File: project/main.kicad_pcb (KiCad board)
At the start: 6 copper layers, 160 x 257 mm, 207 parts

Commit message: extra comms and power towards hallway
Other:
- board text added: "201"
- board text added: "202"
- board text added: "203"
- board text added: "204"
- board text added: "215"
- board text added: "216"
- board text added: "3x2.5 C16 8m 3x"
- board text added: "D313"
- board text added: "PDU-A1 and PDU-A2 - 2x23m"
- board text added: "PDU-B1 and PDU-B2 - 2x16m"
- board text added: "cam-el2 27m"
- board text added: "print-dfm1 21m"
- board text added: "print-dfm2 21m"
- board text added: "print-sla1 17m"
- board text removed: "???"
- board text removed: "PDU-A-1 and PDU-A-2 - 2x22m"
- board text removed: "PDU-B-1 and PDU-B-2 - 2x15m"
- board text removed: "cam-el2 11m"
- board text removed: "print-dfm1 19m"
- board text removed: "print-dfm2 19m"

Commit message: updating ventilation map
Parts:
- added R105: machine intake fan, -local:_q_laser_fan__, F.Cu at (78.3, 43.8)
- added R106: heat exchanger, -local:_q_printers_fan__, F.Cu at (83.8, 165.3)
- added R107: dirty big fan, -local:_q_paint_fan__, F.Cu at (78.3, 97.3)
- R101: value Laser fan -> laser fan
- R102: value Paint fan -> dirty fan
- R103: value Printers fan -> air con
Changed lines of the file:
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@@
   (net 110 "unconnected-(R99-Pad1)")
   (net 111 "unconnected-(R52-Pad1)")
+  (net 112 "unconnected-(R105-Pad1)")
+  (net 113 "unconnected-(R106-Pad1)")
+  (net 114 "unconnected-(R107-Pad1)")
   (footprint "-local:_o_lathe__" (layer "F.Cu")
     (at 112.28 26)
@@
     )
   )
+  (footprint "-local:_q_paint_fan__" (layer "F.Cu")
+    (at 78.28 97.32 90)
+    (property "Sheetfile" "main.kicad_sch")
+    (property "Sheetname" "")
+    (attr smd)
+    (fp_text reference "R107" (at -0.5 -1.5 90 unlocked) (layer "F.Fab")
+      (effects (font (size 0.8 0.8) (thickness 0.08)) (justify left))
+    )
+    (fp_text value "dirty big fan" (at 0.5 3 90 unlocked) (layer "F.SilkS")
+      (effects (font (size 0.8 0.8) (thickness 0.08)) (justify left))
+    )
+    (fp_text user "${REFERENCE}" (at 1.5 -3 90 unlocked) (layer "F.Fab")
+      (effects (font (size 1 1) (thickness 0.15)))
+    )
+    (fp_rect (start 0 0) (end 3 2) (layer "F.SilkS") (width 0.12) (fill none))
+    (fp_rect (start -0.5 -0.5) (end 3.5 2.5) (layer "F.CrtYd") (width 0.05) (fill none))
+    (pad "1" smd roundrect (at 1.5 1 90) (size 3 2) (layers "F.Cu" "F.Paste" "F.Mask") (roundrect_rratio 0.1)
+      (net 114 "unconnected-(R107-Pad1)") (pintype "passive"))
+    (model "${KIPRJMOD}/lib/model/cube_1x1x1_mm.step"
+      (offset (xyz 1.5 -1 15))
+      (scale (xyz 3 2 3))
+      (rotate (xyz 0 0 0))
+    )
+  )
   (footprint "-local:chair_small" (layer "F.Cu")
     (at 148.5 194.25 -90)
@@
       (effects (font (size 0.8 0.8) (thickness 0.08)) (justify left))
     )
-    (fp_text value "Laser fan" (at 0.5 3 90 unlocked) (layer "F.SilkS")
+    (fp_text value "laser fan" (at 0.5 3 90 unlocked) (layer "F.SilkS")
       (effects (font (size 0.8 0.8) (thickness 0.08)) (justify left))
     )
@@
       (effects (font (size 0.8 0.8) (thickness 0.08)) (justify left))
     )
-    (fp_text value "Paint fan" (at 0.5 3 90 unlocked) (layer "F.SilkS")
+    (fp_text value "dirty fan" (at 0.5 3 90 unlocked) (layer "F.SilkS")
       (effects (font (size 0.8 0.8) (thickness 0.08)) (justify left))
     )
@@
     )
   )
+  (footprint "-local:_q_laser_fan__" (layer "F.Cu")
+    (at 78.28 43.82 90)
+    (property "Sheetfile" "main.kicad_sch")
+    (property "Sheetname" "")
+    (attr smd)
+    (fp_text reference "R105" (at -0.5 -1.5 90 unlocked) (layer "F.Fab")
+      (effects (font (size 0.8 0.8) (thickness 0.08)) (justify left))
+    )
+    (fp_text value "machine intake fan" (at 0.5 3 90 unlocked) (layer "F.SilkS")
+      (effects (font (size 0.8 0.8) (thickness 0.08)) (justify left))
+    )
+    (fp_text user "${REFERENCE}" (at 1.5 -3 90 unlocked) (layer "F.Fab")
+      (effects (font (size 1 1) (thickness 0.15)))
+    )
+    (fp_rect (start 0 0) (end 3 2) (layer "F.SilkS") (width 0.12) (fill none))
+    (fp_rect (start -0.5 -0.5) (end 3.5 2.5) (layer "F.CrtYd") (width 0.05) (fill none))
+    (pad "1" smd roundrect (at 1.5 1 90) (size 3 2) (layers "F.Cu" "F.Paste" "F.Mask") (roundrect_rratio 0.1)
+      (net 112 "unconnected-(R105-Pad1)") (pintype "passive"))
+    (model "${KIPRJMOD}/lib/model/cube_1x1x1_mm.step"
+      (offset (xyz 1.5 -1 15))
+      (scale (xyz 3 2 3))
+      (rotate (xyz 0 0 0))
+    )
+  )
   (footprint "-local:chair_small" (layer "F.Cu")
     (at 148.5 199.25 -90)
@@
     )
   )
+  (footprint "-local:_q_printers_fan__" (layer "F.Cu")
+    (at 83.78 165.32)
+    (property "Sheetfile" "main.kicad_sch")
+    (property "Sheetname" "")
+    (attr smd)
+    (fp_text reference "R106" (at -0.5 -1.5 unlocked) (layer "F.Fab")
+      (effects (font (size 0.8 0.8) (thickness 0.08)) (justify left))
+    )
+    (fp_text value "heat exchanger" (at 0.5 3 unlocked) (layer "F.SilkS")
+      (effects (font (size 0.8 0.8) (thickness 0.08)) (justify left))
+    )
+    (fp_text user "${REFERENCE}" (at 1.5 -3 unlocked) (layer "F.Fab")
+      (effects (font (size 1 1) (thickness 0.15)))
+    )
+    (fp_rect (start 0 0) (end 3 2) (layer "F.SilkS") (width 0.12) (fill none))
+    (fp_rect (start -0.5 -0.5) (end 3.5 2.5) (layer "F.CrtYd") (width 0.05) (fill none))
+    (pad "1" smd roundrect (at 1.5 1) (size 3 2) (layers "F.Cu" "F.Paste" "F.Mask") (roundrect_rratio 0.1)
+      (net 113 "unconnected-(R106-Pad1)") (pintype "passive"))
+    (model "${KIPRJMOD}/lib/model/cube_1x1x1_mm.step"
+      (offset (xyz 1.5 -1 15))
+      (scale (xyz 3 2 3))
+      (rotate (xyz 0 0 0))
+    )
+  )
   (footprint "-local:_o_thick_shelf__" (layer "F.Cu")
     (at 196.78 117.87 180)
@@
       (effects (font (size 0.8 0.8) (thickness 0.08)) (justify left))
     )
-    (fp_text value "Printers fan" (at 0.5 3 90 unlocked) (layer "F.SilkS")
+    (fp_text value "air con" (at 0.5 3 90 unlocked) (layer "F.SilkS")
       (effects (font (size 0.8 0.8) (thickness 0.08)) (justify left))
     )
@@
   )
   (gr_line (start 194.28 54.32) (end 194.28 62.32) (layer "In2.Cu") (width 5))
-  (gr_line (start 173.28 176.32) (end 194.28 176.32) (layer "In2.Cu") (width 3))
-  (gr_line (start 173.28 176.32) (end 173.28 172.32) (layer "In2.Cu") (width 3))
-  (gr_line (start 199.28 121.32) (end 194.28 121.32) (layer "In2.Cu") (width 3))
+  (gr_line (start 191.28 179.32) (end 194.28 179.32) (layer "In2.Cu") (width 3))
+  (gr_line (start 191.28 182.32) (end 191.28 179.32) (layer "In2.Cu") (width 3))
+  (gr_line (start 199.28 133.32) (end 194.28 133.32) (layer "In2.Cu") (width 3))
   (gr_line (start 90.28 31.32) (end 90.28 26.32) (layer "In2.Cu") (width 2))
   (gr_line (start 181.28 54.32) (end 194.28 54.32) (layer "In2.Cu") (width 5))
-  (gr_line (start 173.28 180.32) (end 173.28 176.32) (layer "In2.Cu") (width 1))
-  (gr_line (start 173.28 180.32) (end 152.28 180.32) (layer "In2.Cu") (width 1))
+  (gr_line (start 188.28 179.32) (end 191.28 179.32) (layer "In2.Cu") (width 1))
+  (gr_line (start 199.28 71.32) (end 194.28 71.32) (layer "In2.Cu") (width 3))
   (gr_line (start 194.28 62.32) (end 199.28 62.32) (layer "In2.Cu") (width 5))
   (gr_line (start 164.28 31.32) (end 164.28 26.32) (layer "In2.Cu") (width 2))
   (gr_line (start 90.28 31.32) (end 171.28 31.32) (layer "In2.Cu") (width 2))
-  (gr_line (start 171.28 31.32) (end 171.28 53.32) (layer "In2.Cu") (width 2))
-  (gr_line (start 194.28 176.32) (end 194.28 62.32) (layer "In2.Cu") (width 3))
+  (gr_line (start 194.28 179.32) (end 194.28 62.32) (layer "In2.Cu") (width 3))
   (gr_line (start 169.28 26.32) (end 169.28 57.32) (layer "In3.Cu") (width 1))
   (gr_arc (start 119.28 119.32) (mid 116.351068 126.391068) (end 109.28 129.32) (layer "In3.Cu") (width 0.2))
@@
   (gr_line (start 109.28 129.32) (end 109.28 119.32) (layer "In3.Cu") (width 0.2))
   (gr_line (start 201.28 179.82) (end 126.28 179.82) (layer "In3.Cu") (width 0.5))
+  (gr_line (start 196.28 30.32) (end 196.28 60.32) (layer "In4.Cu") (width 1.6))
+  (gr_line (start 196.28 30.32) (end 155.28 30.32) (layer "In4.Cu") (width 1.6))
+  (gr_line (start 156.28 92.32) (end 156.28 63.32) (layer "In4.Cu") (width 2))
+  (gr_line (start 79.28 42.32) (end 84.28 42.32) (layer "In4.Cu") (width 2))
+  (gr_line (start 83.28 155.32) (end 79.28 155.32) (layer "In4.Cu") (width 2.5))
+  (gr_line (start 105.28 173.32) (end 105.28 181.32) (layer "In4.Cu") (width 2))
+  (gr_line (start 87.28 139.32) (end 87.28 164.32) (layer "In4.Cu") (width 2.5))
+  (gr_line (start 87.28 169.32) (end 87.28 168.32) (layer "In4.Cu") (width 2.5))
+  (gr_line (start 87.28 139.32) (end 79.28 139.32) (layer "In4.Cu") (width 2.5))
+  (gr_line (start 136.28 53.32) (end 136.28 50.32) (layer "In4.Cu") (width 0.8))
+  (gr_line (start 83.28 168.32) (end 83.28 173.32) (layer "In4.Cu") (width 2.5))
+  (gr_line (start 84.28 42.32) (end 84.28 31.32) (layer "In4.Cu") (width 2))
+  (gr_line (start 135.28 181.32) (end 197.28 181.32) (layer "In4.Cu") (width 2))
+  (gr_line (start 83.28 181.32) (end 83.28 225.32) (layer "In4.Cu") (width 2))
+  (gr_line (start 79.28 80.32) (end 85.28 80.32) (layer "In4.Cu") (width 2))
+  (gr_line (start 155.28 32.32) (end 155.28 30.32) (layer "In4.Cu") (width 1.6))
+  (gr_line (start 87.28 169.32) (end 135.28 169.32) (layer "In4.Cu") (width 2.5))
+  (gr_line (start 85.28 80.32) (end 85.28 63.32) (layer "In4.Cu") (width 2))
+  (gr_line (start 83.28 173.32) (end 105.28 173.32) (layer "In4.Cu") (width 2.5))
+  (gr_line (start 79.28 76.32) (end 82.28 76.32) (layer "In4.Cu") (width 1.6))
+  (gr_line (start 136.28 53.32) (end 167.28 53.32) (layer "In4.Cu") (width 0.8))
+  (gr_line (start 85.28 63.32) (end 187.28 63.32) (layer "In4.Cu") (width 2))
+  (gr_line (start 167.28 30.32) (end 167.28 53.32) (layer "In4.Cu") (width 0.8))
+  (gr_line (start 83.28 155.32) (end 83.28 164.32) (layer "In4.Cu") (width 2.5))
+  (gr_line (start 198.28 42.32) (end 196.28 42.32) (layer "In4.Cu") (width 1.6))
+  (gr_line (start 135.28 169.32) (end 135.28 181.32) (layer "In4.Cu") (width 2))
+  (gr_line (start 82.28 60.32) (end 82.28 76.32) (layer "In4.Cu") (width 1.6))
+  (gr_line (start 83.28 181.32) (end 105.28 181.32) (layer "In4.Cu") (width 2))
+  (gr_line (start 82.28 60.32) (end 196.28 60.32) (layer "In4.Cu") (width 1.6))
   (gr_rect (start 185.28 273.32) (end 189.28 275.32) (layer "B.Cu") (width 0.15) (fill solid))
   (gr_poly

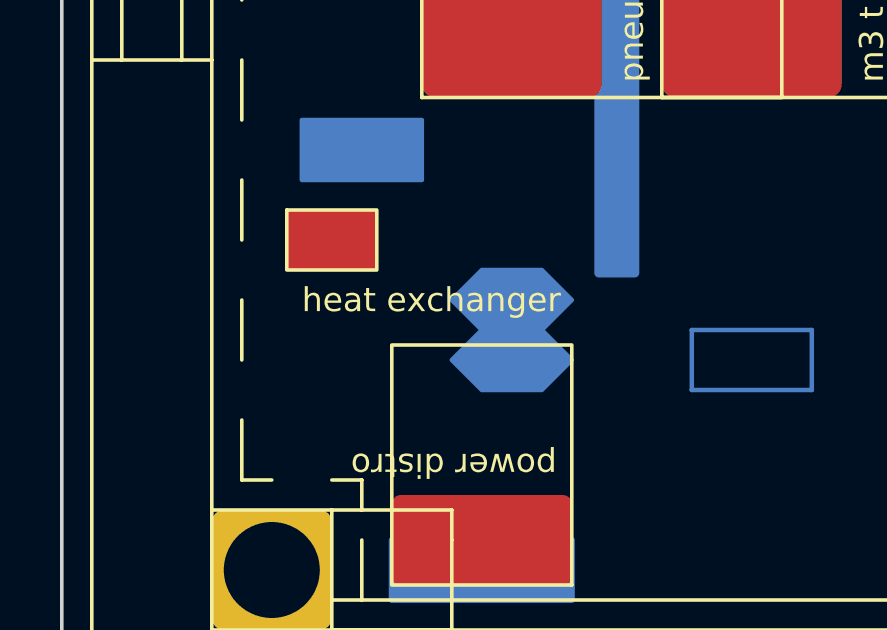
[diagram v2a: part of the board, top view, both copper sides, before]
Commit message: adding permament power for heat exchanger sensors
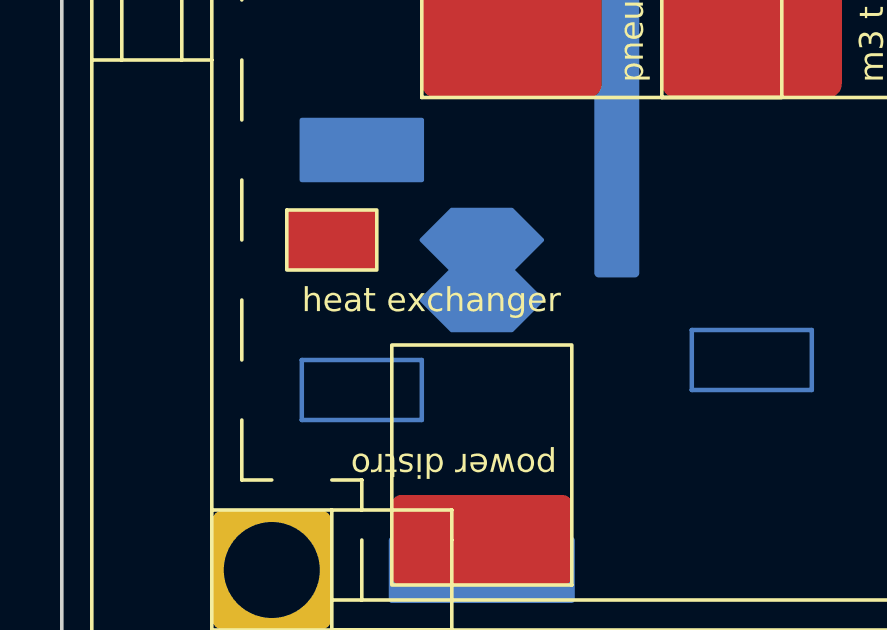
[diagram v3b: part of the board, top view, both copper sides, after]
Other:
- board text added: "3x1 4m sens x1 via P321"
- board text added: "P325"
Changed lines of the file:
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@@
       (xy 128.28 249.32)
     ) (layer "B.Cu") (width 0.15) (fill solid))
+  (gr_rect (start 84.28 172.32) (end 88.28 170.32) (layer "B.Cu") (width 0.15) (fill none))
   (gr_rect (start 144.28 234.32) (end 148.28 236.32) (layer "B.Cu") (width 0.15) (fill solid))
   (gr_poly
@@
   (gr_poly
     (pts
-      (xy 93.28 170.32)
-      (xy 92.28 171.32)
-      (xy 90.28 171.32)
-      (xy 89.28 170.32)
-      (xy 90.28 169.32)
-      (xy 92.28 169.32)
+      (xy 92.28 168.32)
+      (xy 91.28 169.32)
+      (xy 89.28 169.32)
+      (xy 88.28 168.32)
+      (xy 89.28 167.32)
+      (xy 91.28 167.32)
     ) (layer "B.Cu") (width 0.15) (fill solid))
   (gr_rect (start 84.28 85.32) (end 88.28 87.32) (layer "B.Cu") (width 0.15) (fill solid))
@@
   (gr_poly
     (pts
-      (xy 93.28 168.32)
-      (xy 92.28 169.32)
-      (xy 90.28 169.32)
-      (xy 89.28 168.32)
-      (xy 90.28 167.32)
-      (xy 92.28 167.32)
+      (xy 92.28 166.32)
+      (xy 91.28 167.32)
+      (xy 89.28 167.32)
+      (xy 88.28 166.32)
+      (xy 89.28 165.32)
+      (xy 91.28 165.32)
     ) (layer "B.Cu") (width 0.15) (fill solid))
   (gr_rect (start 142.28 232.32) (end 146.28 230.32) (layer "B.Cu") (width 0.15) (fill none))
@@
   (gr_line (start 181.28 246.32) (end 181.28 245.32) (layer "User.4") (width 0.15))
   (gr_line (start 209.28 48.32) (end 203.28 48.32) (layer "User.4") (width 0.15))
+  (gr_line (start 83.28 171.32) (end 82.28 172.32) (layer "User.4") (width 0.15))
   (gr_line (start 146.28 179.32) (end 145.28 180.32) (layer "User.4") (width 0.15))
   (gr_line (start 195.28 249.32) (end 195.28 250.32) (layer "User.4") (width 0.15))
@@
   (gr_line (start 107.28 228.32) (end 106.28 229.32) (layer "User.4") (width 0.15))
   (gr_line (start 79.28 77.32) (end 80.28 78.32) (layer "User.4") (width 0.15))
+  (gr_line (start 82.28 171.32) (end 82.28 170.32) (layer "User.4") (width 0.15))
   (gr_line (start 113.28 48.32) (end 114.28 48.32) (layer "User.4") (width 0.15))
   (gr_line (start 106.28 109.32) (end 105.28 108.32) (layer "User.4") (width 0.15))
@@
   (gr_line (start 105.28 228.32) (end 106.28 228.32) (layer "User.4") (width 0.15))
   (gr_line (start 79.28 43.32) (end 79.28 42.32) (layer "User.4") (width 0.15))
-  (gr_line (start 62.28 120.32) (end 74.28 120.32) (layer "User.4") (width 0.15))
+  (gr_line (start 73.28 120.32) (end 74.28 120.32) (layer "User.4") (width 0.15))
   (gr_line (start 144.28 179.32) (end 145.28 179.32) (layer "User.4") (width 0.15))
   (gr_line (start 79.28 67.32) (end 79.28 66.32) (layer "User.4") (width 0.15))
@@
   (gr_line (start 105.28 108.32) (end 106.28 108.32) (layer "User.4") (width 0.15))
   (gr_line (start 209.28 111.32) (end 203.28 111.32) (layer "User.4") (width 0.15))
+  (gr_line (start 82.28 170.32) (end 83.28 171.32) (layer "User.4") (width 0.15))
   (gr_line (start 207.28 193.32) (end 208.28 192.32) (layer "User.4") (width 0.15))
   (gr_line (start 208.28 206.32) (end 207.28 205.32) (layer "User.4") (width 0.15))
+  (gr_line (start 73.28 171.32) (end 82.28 171.32) (layer "User.4") (width 0.15))
   (gr_line (start 179.78 264.32) (end 180.78 265.32) (layer "User.4") (width 0.15))
   (gr_line (start 145.28 189.32) (end 146.28 190.32) (layer "User.4") (width 0.15))
@@
   (gr_line (start 146.28 59.32) (end 145.28 60.32) (layer "User.4") (width 0.15))
   (gr_line (start 77.28 184.32) (end 79.28 184.32) (layer "User.4") (width 0.15))
+  (gr_line (start 82.28 172.32) (end 82.28 171.32) (layer "User.4") (width 0.15))
   (gr_line (start 78.28 33.32) (end 79.28 33.32) (layer "User.4") (width 0.15))
   (gr_line (start 201.28 250.32) (end 195.28 250.32) (layer "User.4") (width 0.15))
   (gr_line (start 170.28 186.32) (end 169.28 185.32) (layer "User.4") (width 0.15))
   (gr_line (start 180.28 33.32) (end 174.28 33.32) (layer "User.4") (width 0.15))
-  (gr_line (start 62.28 181.32) (end 74.28 181.32) (layer "User.4") (width 0.15))
+  (gr_line (start 73.28 181.32) (end 74.28 181.32) (layer "User.4") (width 0.15))
   (gr_line (start 74.28 181.32) (end 77.28 184.32) (layer "User.4") (width 0.15))
   (gr_line (start 114.28 48.32) (end 115.28 48.32) (layer "User.4") (width 0.15))
@@
   (gr_line (start 115.28 83.32) (end 114.28 84.32) (layer "User.5") (width 0.15))
   (gr_line (start 128.28 188.32) (end 127.28 189.32) (layer "User.5") (width 0.15))
-  (gr_line (start 87.28 168.32) (end 88.28 169.32) (layer "User.5") (width 0.15))
+  (gr_line (start 86.28 167.32) (end 87.28 168.32) (layer "User.5") (width 0.15))
   (gr_line (start 128.28 210.32) (end 129.28 209.32) (layer "User.5") (width 0.15))
   (gr_line (start 160.28 66.32) (end 158.28 66.32) (layer "User.5") (width 0.15))
@@
   (gr_line (start 207.28 187.32) (end 208.28 186.32) (layer "User.5") (width 0.15))
   (gr_line (start 174.28 235.32) (end 174.28 237.32) (layer "User.5") (width 0.15))
-  (gr_line (start 88.28 169.32) (end 87.28 170.32) (layer "User.5") (width 0.15))
+  (gr_line (start 87.28 168.32) (end 86.28 169.32) (layer "User.5") (width 0.15))
   (gr_line (start 128.28 253.32) (end 127.28 252.32) (layer "User.5") (width 0.15))
   (gr_line (start 207.28 184.32) (end 208.28 183.32) (layer "User.5") (width 0.15))
@@
   (gr_line (start 126.28 253.32) (end 127.28 252.32) (layer "User.5") (width 0.15))
   (gr_line (start 118.28 42.32) (end 119.28 41.32) (layer "User.5") (width 0.15))
-  (gr_line (start 74.28 169.32) (end 87.28 169.32) (layer "User.5") (width 0.15))
+  (gr_line (start 73.28 168.32) (end 86.28 168.32) (layer "User.5") (width 0.15))
   (gr_line (start 80.28 149.32) (end 79.28 150.32) (layer "User.5") (width 0.15))
   (gr_line (start 92.28 245.32) (end 92.28 238.82) (layer "User.5") (width 0.15))
-  (gr_line (start 87.28 169.32) (end 87.28 170.32) (layer "User.5") (width 0.15))
+  (gr_line (start 86.28 168.32) (end 86.28 169.32) (layer "User.5") (width 0.15))
   (gr_line (start 149.28 190.82) (end 150.28 189.82) (layer "User.5") (width 0.15))
   (gr_line (start 173.28 36.32) (end 174.28 35.32) (layer "User.5") (width 0.15))
@@
   (gr_line (start 92.28 238.82) (end 93.28 238.82) (layer "User.5") (width 0.15))
   (gr_line (start 179.28 184.32) (end 180.28 183.32) (layer "User.5") (width 0.15))
-  (gr_line (start 87.28 169.32) (end 87.28 168.32) (layer "User.5") (width 0.15))
+  (gr_line (start 86.28 168.32) (end 86.28 167.32) (layer "User.5") (width 0.15))
   (gr_line (start 173.28 50.32) (end 174.28 49.32) (layer "User.5") (width 0.15))
   (gr_line (start 150.28 190.82) (end 150.28 198.32) (layer "User.5") (width 0.15))
@@
     (effects (font (size 1 1) (thickness 0.15)) (justify left))
   )
+  (gr_text "3x1 4m sens x1 via P321" (at 73.28 171.32) (layer "User.4")
+    (effects (font (size 2 2) (thickness 0.3)) (justify right))
+  )
   (gr_text "38" (at 200.28 112.32) (layer "User.4")
     (effects (font (size 1 1) (thickness 0.15)) (justify left))
@@
     (effects (font (size 1 1) (thickness 0.15)) (justify left))
   )
-  (gr_text "3x1 11m\nsens x1\nvia P321" (at 61.28 125.32) (layer "User.4")
-    (effects (font (size 2 2) (thickness 0.3)) (justify left))
+  (gr_text "3x1 11m sens x1 via P321" (at 73.28 120.32) (layer "User.4")
+    (effects (font (size 2 2) (thickness 0.3)) (justify right))
   )
   (gr_text "3x2.5 6m via P524 fridge 1x" (at 201.28 250.32) (layer "User.4")
@@
     (effects (font (size 1 1) (thickness 0.15)) (justify left))
   )
-  (gr_text "3x1 11m\nsens x1\nvia P421" (at 60.28 176.32) (layer "User.4")
-    (effects (font (size 2 2) (thickness 0.3)) (justify left))
+  (gr_text "3x1 11m sens x1 via P421" (at 73.28 181.32) (layer "User.4")
+    (effects (font (size 2 2) (thickness 0.3)) (justify right))
   )
   (gr_text "9" (at 115.28 252.32) (layer "User.4")
@@
   (gr_text "3x1 11m sens\nvia P321 x1" (at 150.28 117.32) (layer "User.4")
     (effects (font (size 2 2) (thickness 0.3)) (justify left))
+  )
+  (gr_text "P325" (at 84.28 171.32) (layer "User.4")
+    (effects (font (size 1 1) (thickness 0.15)) (justify left))
   )
   (gr_text "3x1\nB2\n21m\nsens\nx1" (at 100.28 159.32) (layer "User.4")
@@
     (effects (font (size 1 1) (thickness 0.15)) (justify left))
   )
-  (gr_text "PDU-B1 and PDU-B2 - 2x16m" (at 74.28 169.32) (layer "User.5")
+  (gr_text "PDU-B1 and PDU-B2 - 2x16m" (at 73.28 168.32) (layer "User.5")
     (effects (font (size 2 2) (thickness 0.3)) (justify right))
   )
@@
     (effects (font (size 1 1) (thickness 0.15)))
   )
-  (gr_text "204" (at 91.28 170.32) (layer "User.5")
+  (gr_text "204" (at 90.28 168.32) (layer "User.5")
     (effects (font (size 1 1) (thickness 0.15)))
   )
@@
     (effects (font (size 1 1) (thickness 0.15)) (justify left))
   )
-  (gr_text "203" (at 91.28 168.32) (layer "User.5")
-    (effects (font (size 1 1) (thickness 0.15)))
-  )
+  (gr_text "203" (at 90.28 166.32) (layer "User.5")
+    (effects (font (size 1 1) (thickness 0.15)))
+  )
